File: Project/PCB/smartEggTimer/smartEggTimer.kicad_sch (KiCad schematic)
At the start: 64 parts, among them J1 Conn_01x05_Pin, J2 Conn_01x02_Pin, J3 Conn_01x02_Pin, J4 Conn_01x06_Pin, J5 Conn_01x02_Socket, J6 Conn_01x02_Socket, J7 Conn_01x03_Pin, J8 Conn_01x03_Pin, Q1 STP60NF06L, SW1 SW_Push_Dual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

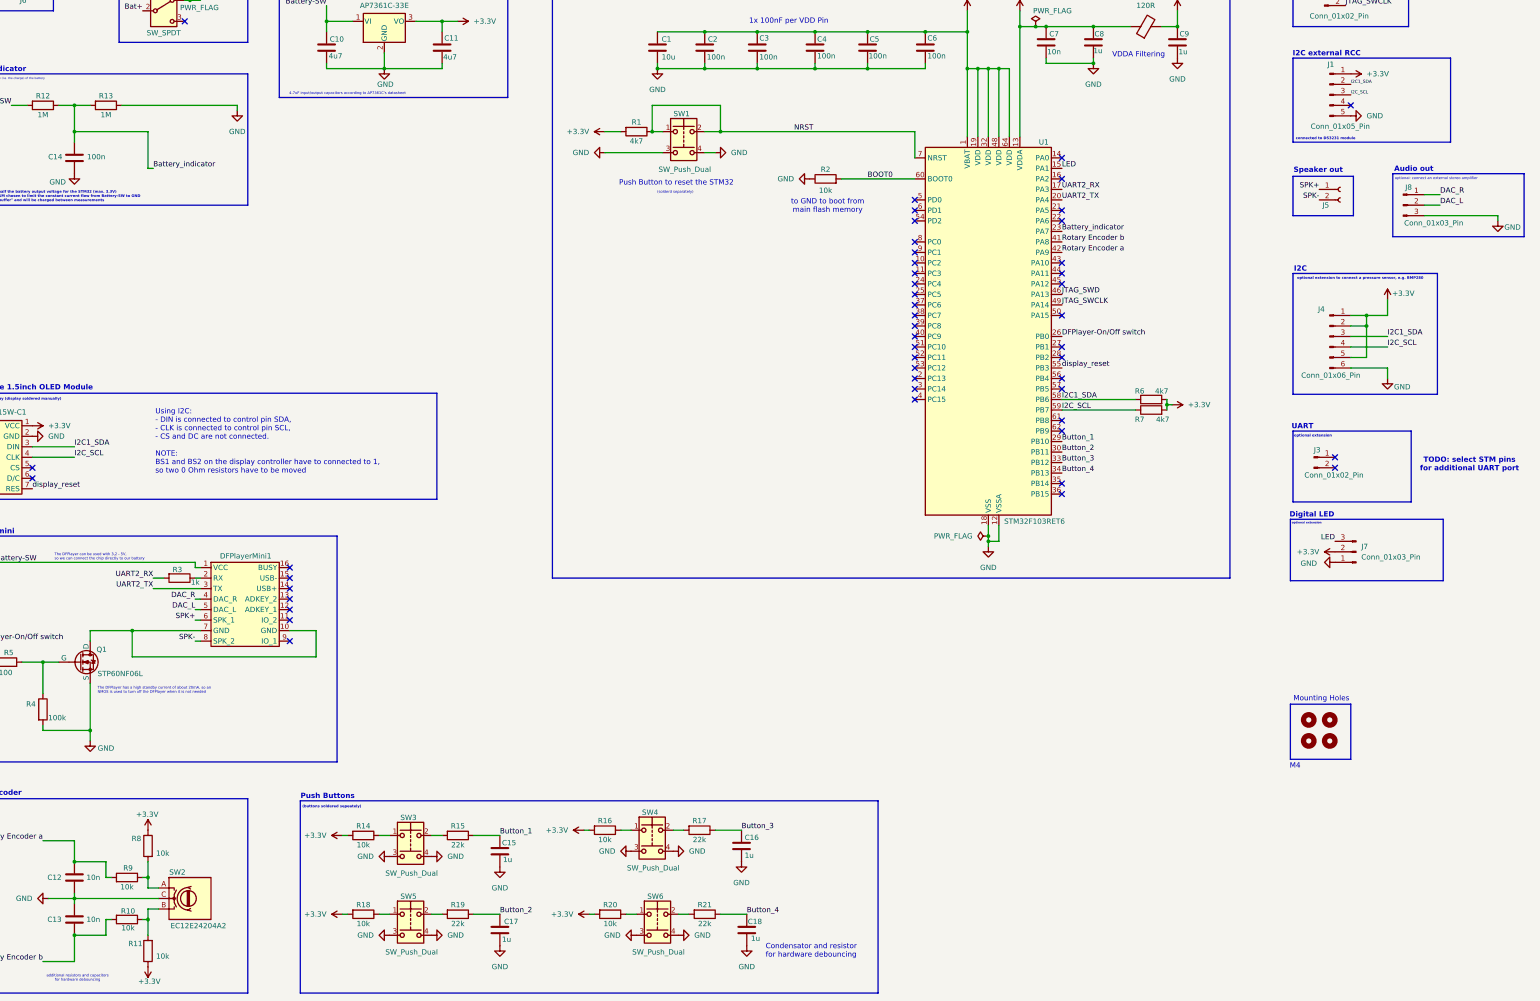
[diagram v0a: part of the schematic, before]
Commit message: add another UART interface
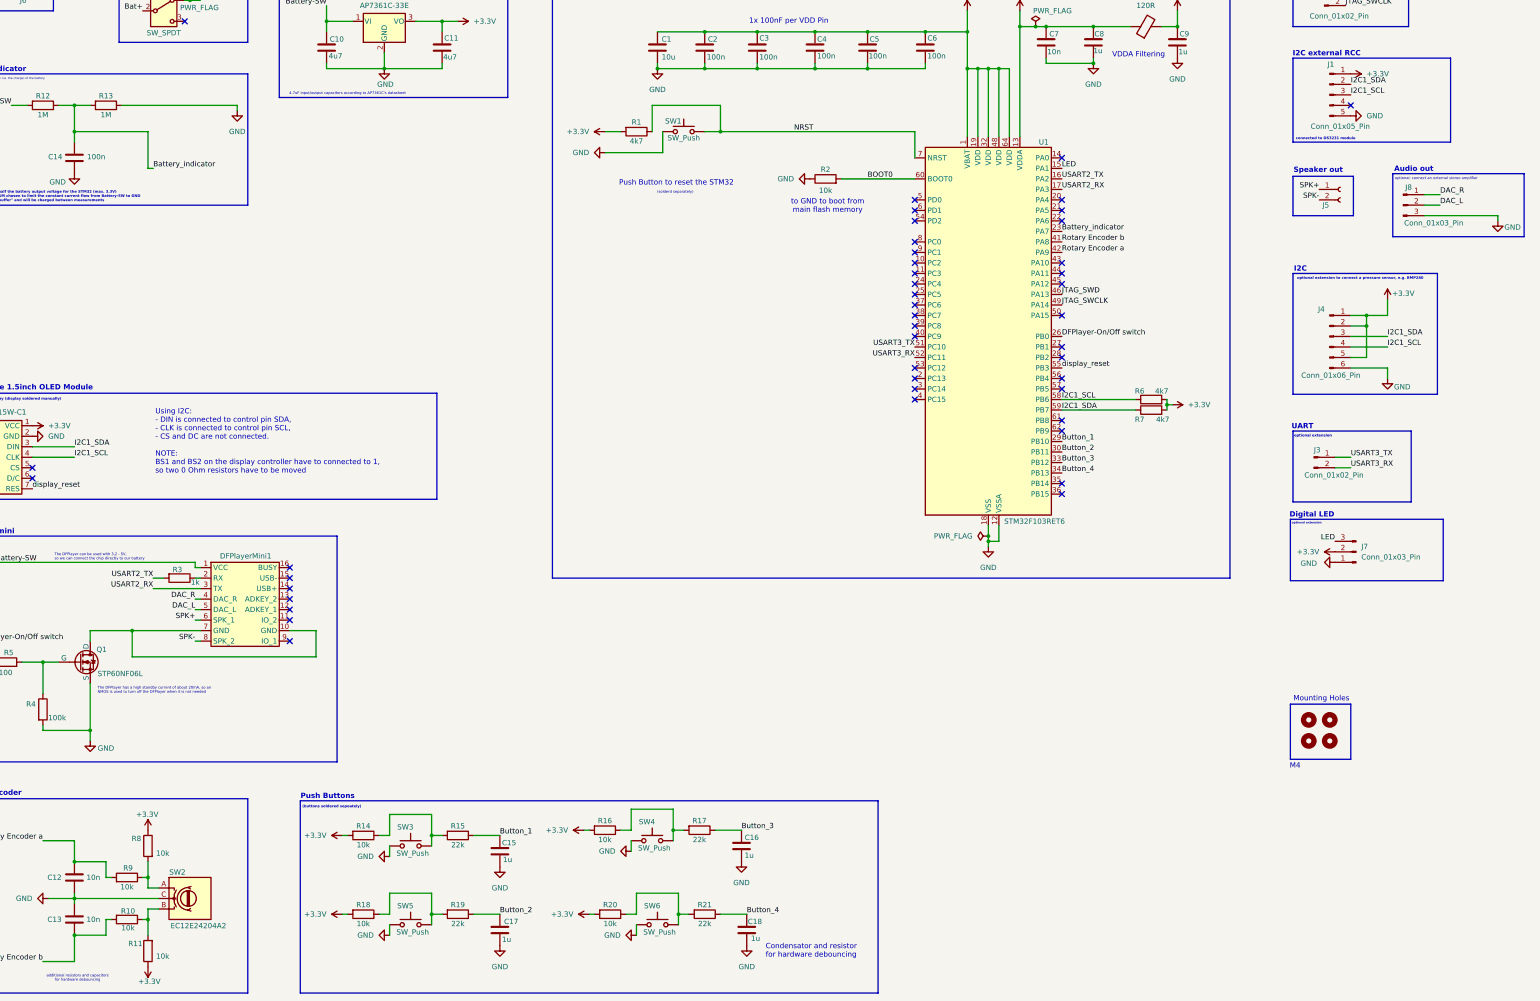
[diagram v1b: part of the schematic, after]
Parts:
- removed SW1: SW_Push_Dual, Button_Switch_THT:SW_PUSH_6mm_H9.5mm, symbol Switch:SW_Push_Dual
- removed SW3, SW4, SW5, SW6: SW_Push_Dual, Button_Switch_THT:SW_PUSH_6mm_H13mm, symbol Switch:SW_Push_Dual
- added SW1: SW_Push, Button_Switch_THT:SW_PUSH_6mm, symbol Switch:SW_Push
- added SW3, SW4, SW5, SW6: SW_Push, Button_Switch_THT:SW_PUSH_6mm_H13mm, symbol Switch:SW_Push
- C10, C11: footprint Capacitor_SMD:C_0603_1608Metric -> Capacitor_SMD:C_0805_2012Metric
- C12, C13, C7: footprint Capacitor_SMD:C_0805_2012Metric -> Capacitor_SMD:C_0402_1005Metric
- C15, C16, C17, C18, C8, C9: footprint Capacitor_SMD:C_0603_1608Metric -> Capacitor_SMD:C_0402_1005Metric
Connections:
- net GND: now also SW1.1, SW3.1, SW4.1, SW5.1, SW6.1
- net I2C1_SDA: now also R7.1, U1.59 (PB7); no longer R6.1, U1.58 (PB6)
- net NRST: now also SW1.2
- net at R15.2: now also R14.1, SW3.2
- net at R19.2: now also R18.1, SW5.2
- net at R16.1: now also R17.2, SW4.2
- net USART2_TX: now reaches U1.16 (PA2)
- net USART2_TX: now also R3.2
- net USART3_TX: now reaches U1.51 (PC10)
- net USART3_TX: now also J3.1 (Pin_1)
- net USART3_RX: now reaches U1.52 (PC11)
- net USART3_RX: now also J3.2 (Pin_2)
- net at R20.1: now also R21.2, SW6.2
- net I2C_SCL renamed I2C1_SCL
- net I2C1_SCL: now also R6.1, U1.58 (PB6); no longer R7.1, U1.59 (PB7)
- net UART2_RX renamed USART2_RX
- net USART2_RX: now also DFPlayerMini1.3 (TX); no longer R3.2
- net UART2_TX: no longer names the net of U1.20 (PA4)
- net UART2_TX: no longer DFPlayerMini1.3 (TX)
- no-connect marks 48 -> 44
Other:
- note removed: "TODO: select STM pins for additional UART port"

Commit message: add GND pins for SWD and optional UART
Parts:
- removed J2, J3: Conn_01x02_Pin, Connector_PinHeader_2.54mm:PinHeader_1x02_P2.54mm_Vertical, symbol Connector:Conn_01x02_Pin
- added J2, J3: Conn_01x03_Pin, Connector_PinHeader_2.54mm:PinHeader_1x03_P2.54mm_Vertical, symbol Connector:Conn_01x03_Pin
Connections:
- net GND: now also J2.3 (Pin_3), J3.3 (Pin_3)
- net JTAG_SWCLK: now also J2.2 (Pin_2)
- net JTAG_SWD: now also J2.1 (Pin_1)
- net USART3_RX: now also J3.2 (Pin_2)
- net USART3_TX: now also J3.1 (Pin_1)
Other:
- note added: "voltage divider to half the battery output voltage for the STM32 (max. 3.6V) high resistance of 1M chosen to limit the constant current flow from Battery-SW to GND capacitor acts as "buffer" and will be charged between measurements"
- note removed: "voltage divider to half the battery output voltage for the STM32 (max. 3.3V) high resistance of 1M chosen to limit the constant current flow from Battery-SW to GND capacitor acts as "buffer" and will be charged between measurements"
- moved on the sheet: J1, J5, J8

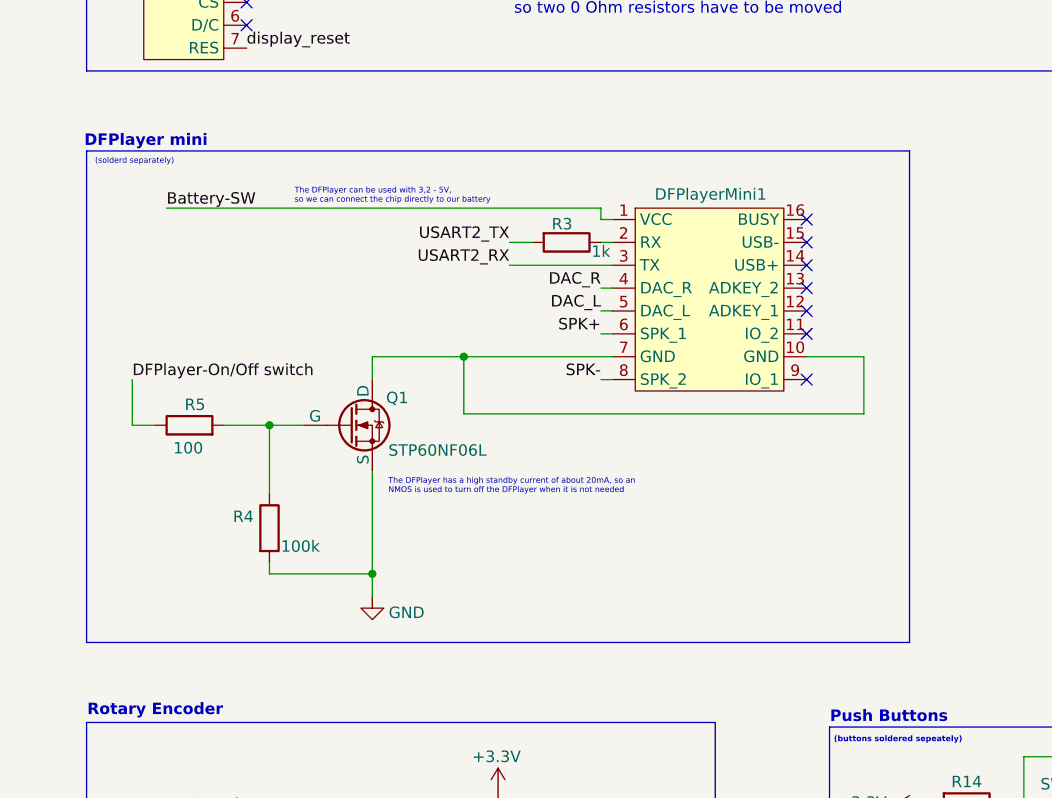
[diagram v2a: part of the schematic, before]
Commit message: rework DFPlayer section based on prototyping - add pull-up resistors for UART communication - add a pin header for the input voltage
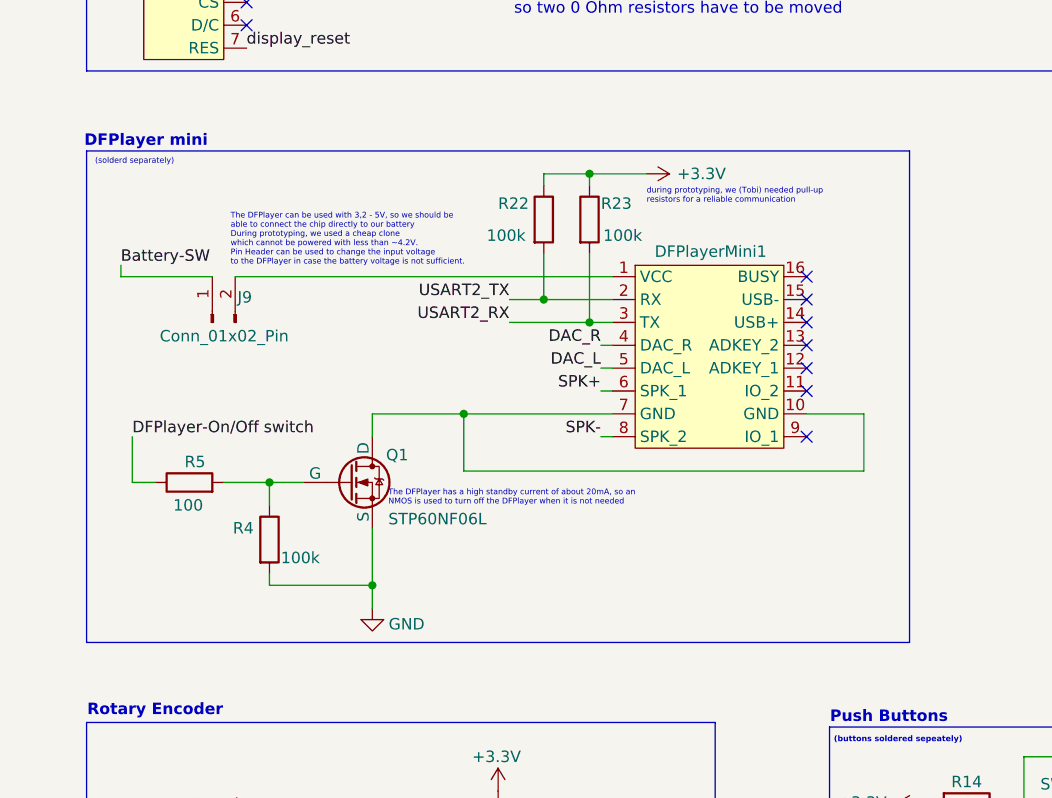
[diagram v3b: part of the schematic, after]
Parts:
- removed R3: 1k, Resistor_SMD:R_0402_1005Metric, symbol Device:R
- added J9: Conn_01x02_Pin, Connector_PinHeader_2.54mm:PinHeader_1x02_P2.54mm_Vertical, symbol Connector:Conn_01x02_Pin
- added R22, R23: 100k, Resistor_SMD:R_0402_1005Metric, symbol Device:R
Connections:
- net +3.3V: now also R22.1, R23.1
- net Battery-SW: now also J9.1 (Pin_1); no longer DFPlayerMini1.1 (VCC)
- net USART2_RX: now also R23.2
- net USART2_TX: now also DFPlayerMini1.2 (RX), R22.2
- new net: DFPlayerMini1.1 (VCC), J9.2 (Pin_2)
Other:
- note added: "The DFPlayer can be used with 3,2 - 5V, so we should be able to connect the chip directly to our battery During prototyping, we used a cheap clone which cannot be powered with less than ~4.2V. Pin Header can be used to change the input voltage to the DFPlayer in case the battery voltage is not sufficient."
- note added: "during prototyping, we (Tobi) needed pull-up resistors for a reliable communication"
- note removed: "The DFPlayer can be used with 3,2 - 5V, so we can connect the chip directly to our battery"
- moved on the sheet: DFPlayerMini1, Q1, R4, R5

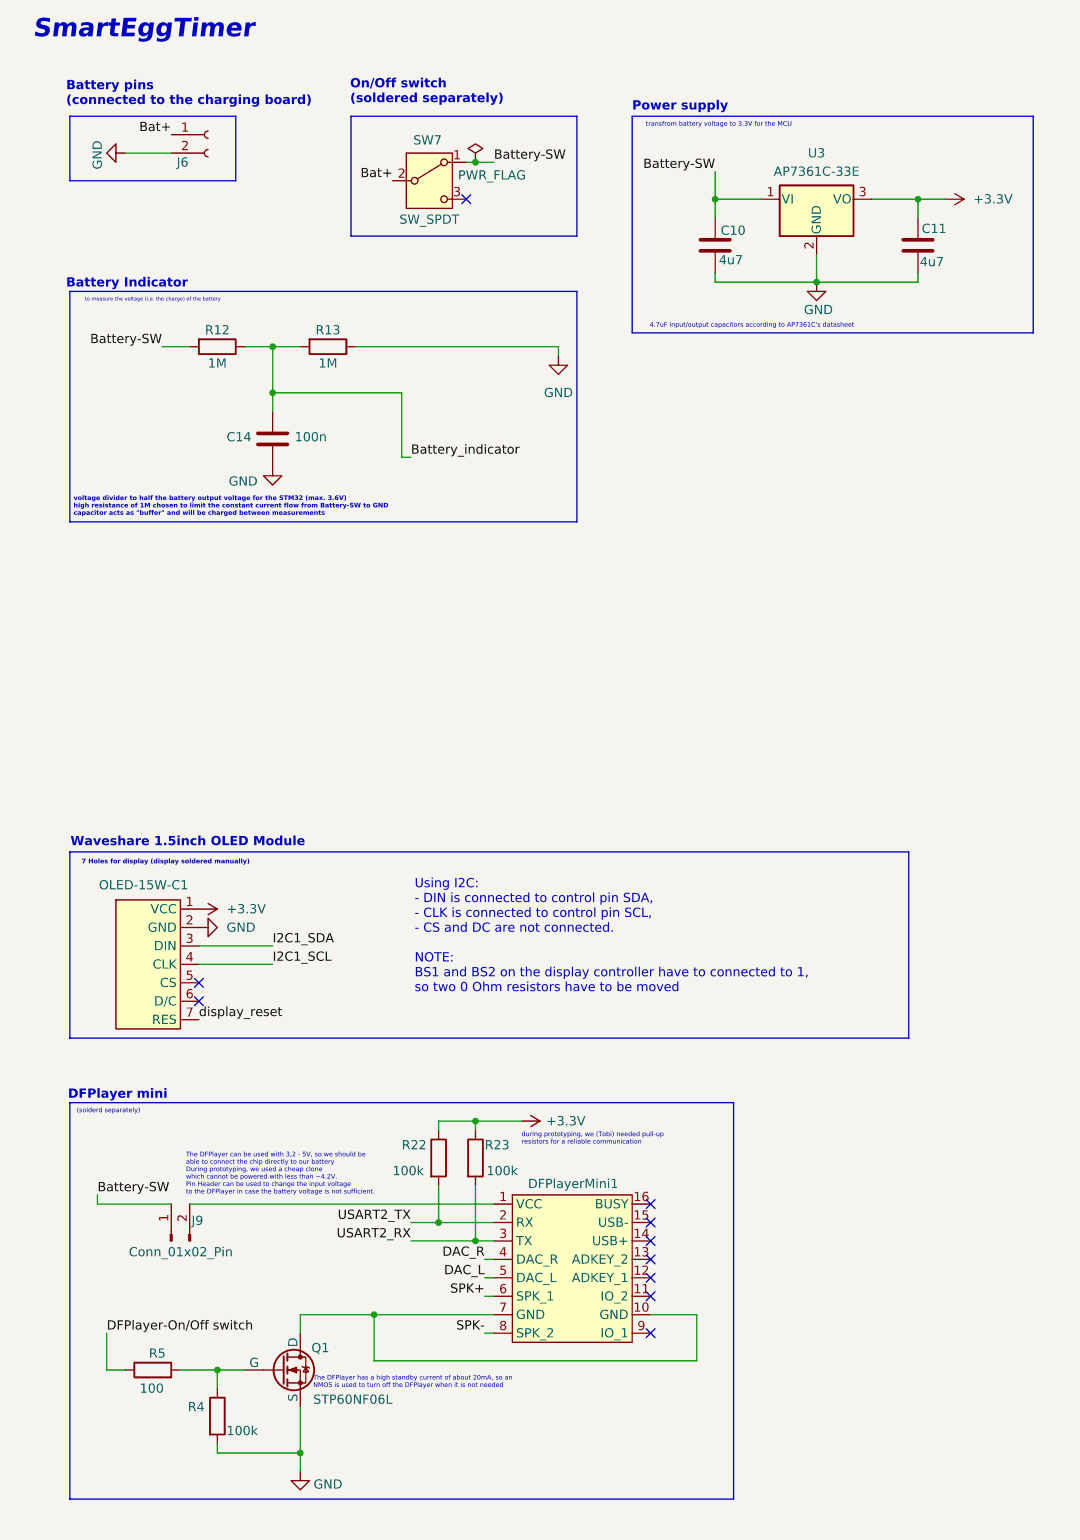
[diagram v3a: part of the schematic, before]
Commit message: placement of all components & initial routing
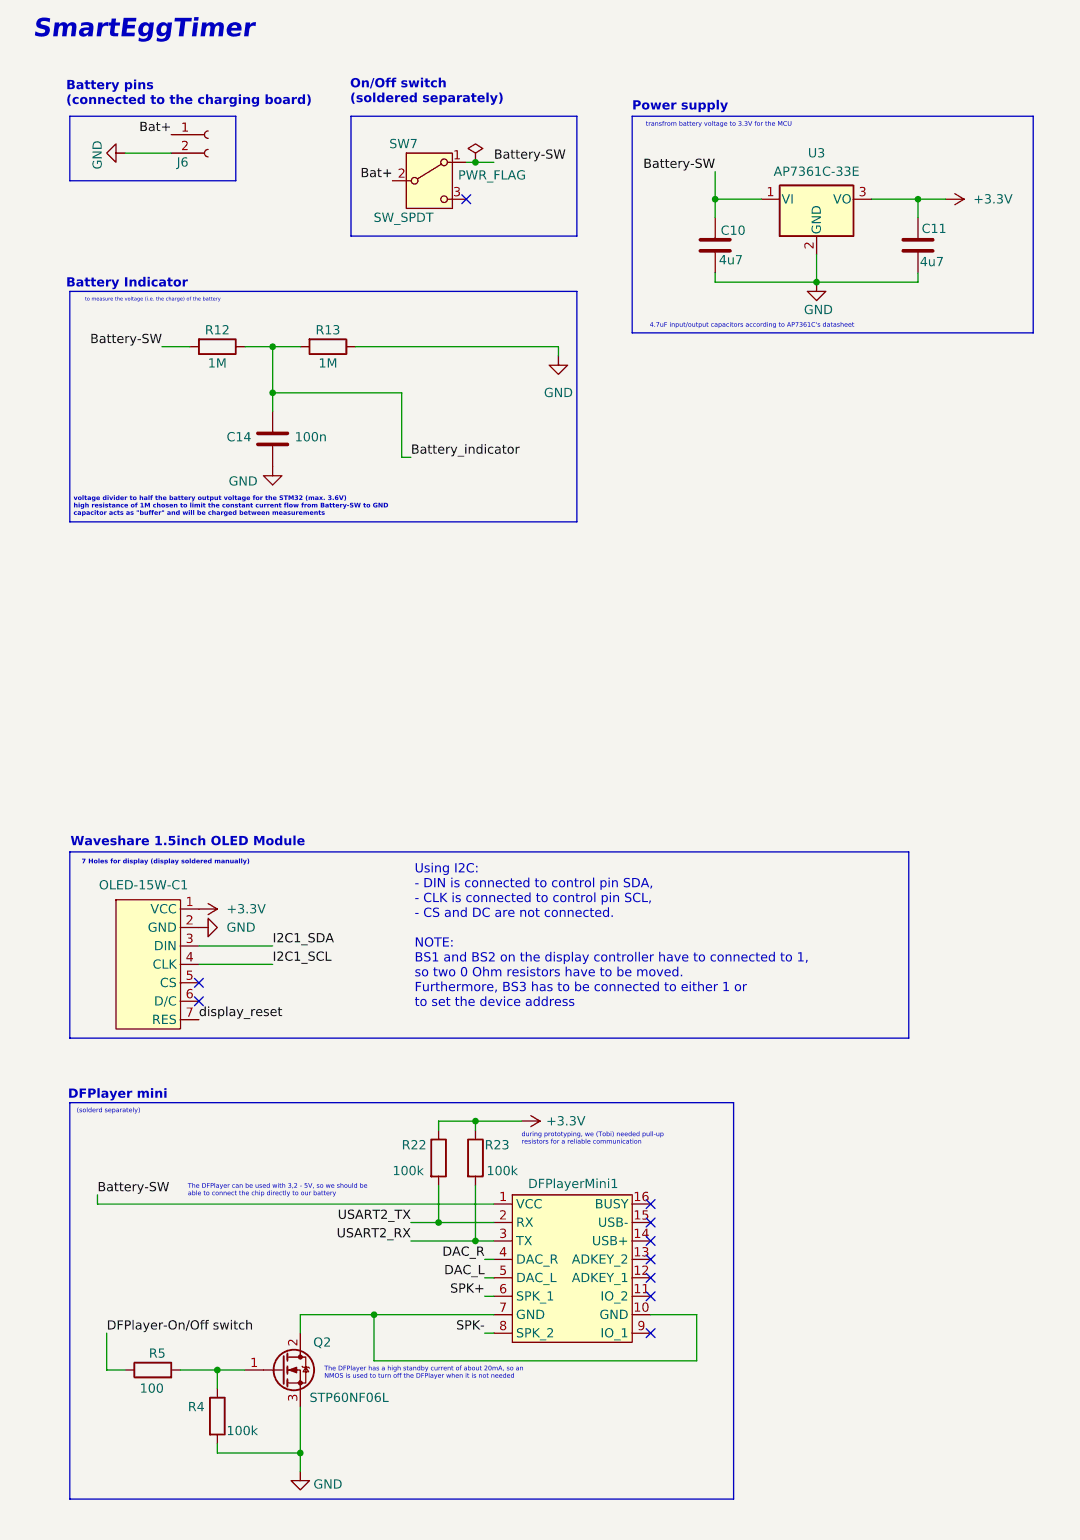
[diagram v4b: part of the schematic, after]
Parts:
- removed J9: Conn_01x02_Pin, Connector_PinHeader_2.54mm:PinHeader_1x02_P2.54mm_Vertical, symbol Connector:Conn_01x02_Pin
- removed Q1: STP60NF06L, Package_TO_SOT_THT:TO-220-3_Vertical, symbol Simulation_SPICE:NMOS
- added Q2: STP60NF06L, Package_TO_SOT_THT:TO-220-3_Vertical, symbol Device:Q_NMOS_GDS
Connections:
- net Battery-SW: now also DFPlayerMini1.1 (VCC)
- net GND: now also Q2.3 (S)
- net at DFPlayerMini1.10 (GND), DFPlayerMini1.7 (GND): now also Q2.2 (D)
- net at R4.1, R5.2: now also Q2.1 (G)
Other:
- note added: "The DFPlayer can be used with 3,2 - 5V, so we should be able to connect the chip directly to our battery"
- note added: "Using I2C: - DIN is connected to control pin SDA, - CLK is connected to control pin SCL, - CS and DC are not connected. NOTE: BS1 and BS2 on the display controller have to connected to 1, so two 0 Ohm resistors have to be moved. Furthermore, BS3 has to be connected to either 1 or to set the device address"
- note removed: "The DFPlayer can be used with 3,2 - 5V, so we should be able to connect the chip directly to our battery During prototyping, we used a cheap clone which cannot be powered with less than ~4.2V. Pin Header can be used to change the input voltage to the DFPlayer in case the battery voltage is not sufficient."
- note removed: "Using I2C: - DIN is connected to control pin SDA, - CLK is connected to control pin SCL, - CS and DC are not connected. NOTE: BS1 and BS2 on the display controller have to connected to 1, so two 0 Ohm resistors have to be moved"
